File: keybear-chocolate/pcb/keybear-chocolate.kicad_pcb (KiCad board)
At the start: 2 copper layers, 151.4 x 117.1 mm, 95 parts, among them J1 MJ-4PP-9, J2 BATT, J3 LED, J4 OLED, SW1 SW_PUSH, SW10 SW_PUSH, SW11 SW_PUSH, SW12 SW_PUSH, SW13 SW_PUSH, SW14 SW_PUSH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

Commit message: adding more tracks
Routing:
- net VCC: track 2.64 -> 465.5 mm, vias 0 -> 25
- net Net-(L14-DIN): track 0.00 -> 39.0 mm, vias 0 -> 4
- net Net-(L14-DOUT): track 38.8 -> 53.7 mm, vias 2 -> 4
- net col2: track 215.5 -> 201.8 mm, vias 8 -> 7
- net Net-(L2-DIN): track 39.9 -> 46.3 mm, vias 2 -> 3
- net col0: track 238.3 -> 233.5 mm, vias 8 -> 7
- net col1: track 200.1 -> 195.7 mm, vias 8 -> 7
- net row2: track 182.1 -> 184.9 mm
- net row1: track 164.4 -> 162.2 mm
- net col4: track 148.2 -> 146.3 mm, vias 8 -> 7
- net ENCB: track 23.6 -> 21.9 mm
- net Net-(L1-DOUT): track 36.4 -> 35.1 mm
- net col3: track 154.6 -> 153.7 mm, vias 10 -> 9
- net Net-(L13-DIN): track 36.8 -> 35.9 mm
- net row0: track 177.3 -> 176.5 mm

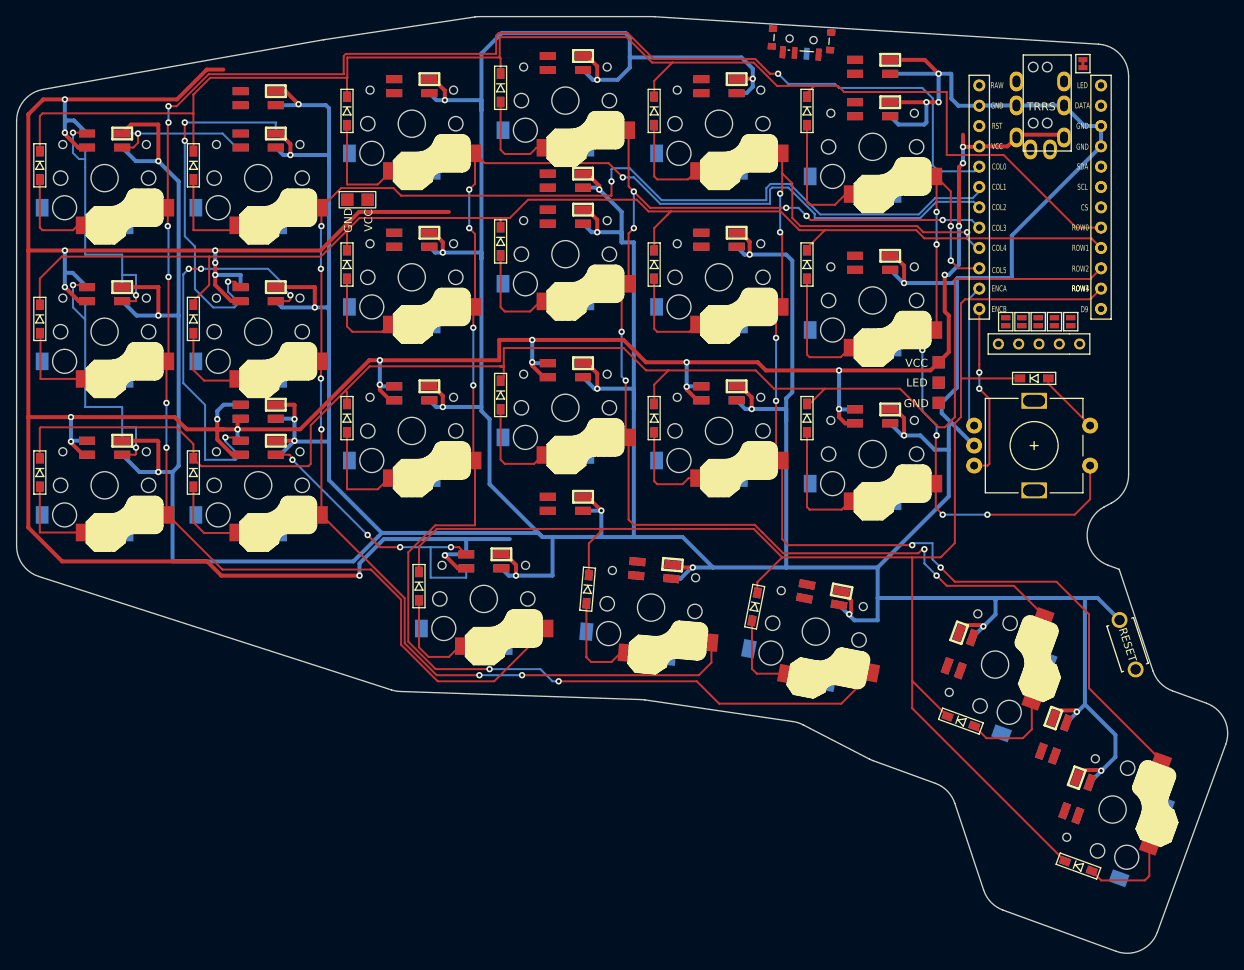
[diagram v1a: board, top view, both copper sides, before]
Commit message: more tracks added
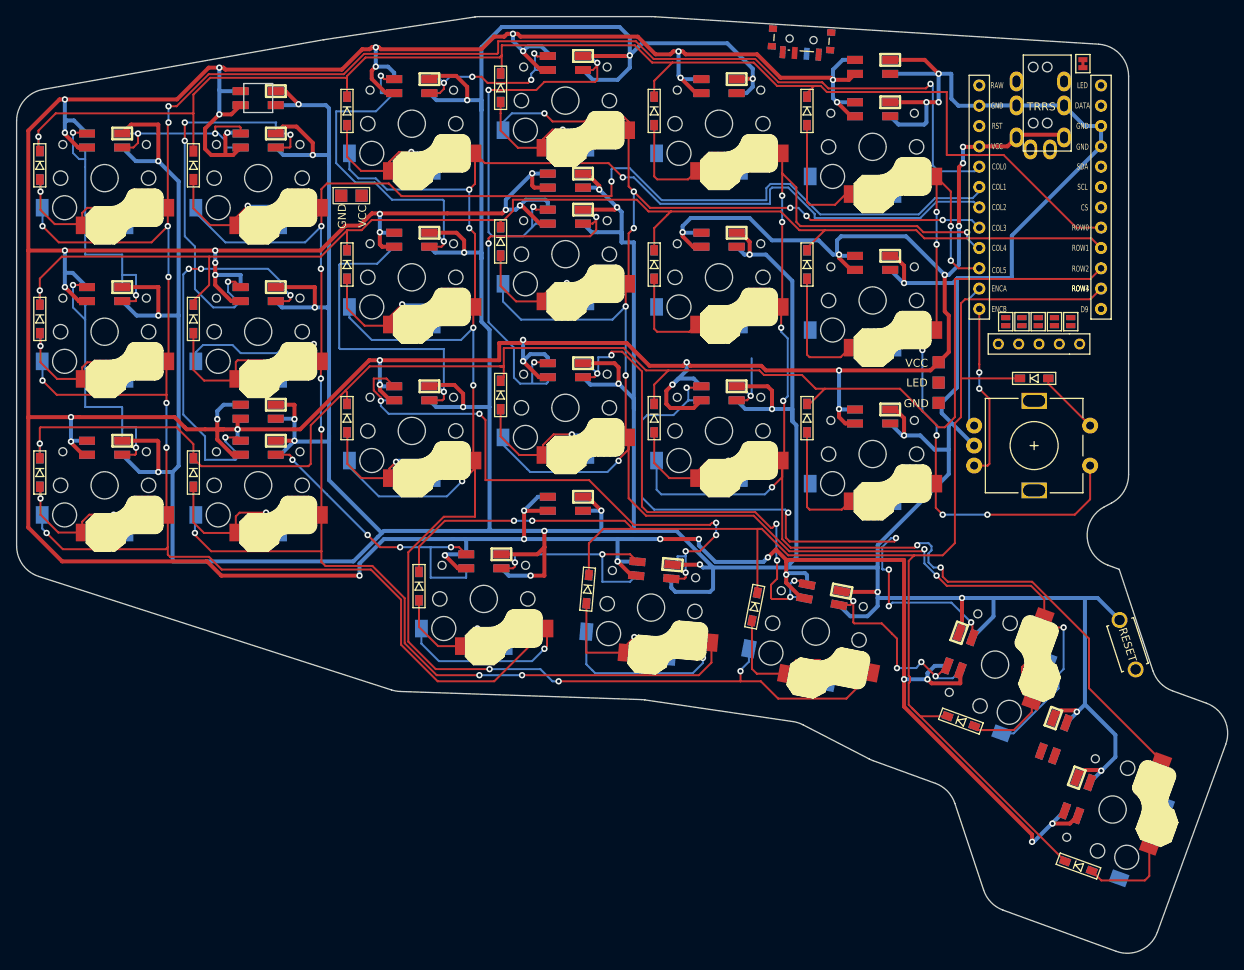
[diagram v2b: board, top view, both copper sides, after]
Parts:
- moved J2 0.92 mm to (179.6, 113.8)
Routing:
- net VCC: track 465.5 -> 861.8 mm, vias 25 -> 54
- net col1: track 195.7 -> 281.9 mm, vias 7 -> 10
- net Net-(L17-DOUT): track 0.00 -> 84.3 mm, vias 0 -> 6
- net col0: track 233.5 -> 313.5 mm, vias 7 -> 11
- net col3: track 153.7 -> 232.6 mm, vias 9 -> 12
- net Net-(L15-DOUT): track 0.00 -> 75.0 mm, vias 0 -> 6
- net Net-(L16-DIN): track 0.00 -> 67.0 mm, vias 0 -> 6
- net col2: track 201.8 -> 262.4 mm, vias 7 -> 9
- net Net-(L10-DOUT): track 0.00 -> 51.6 mm, vias 0 -> 3
- net Net-(L10-DIN): track 0.00 -> 48.3 mm, vias 0 -> 3
- net Net-(L3-DOUT): track 0.00 -> 45.8 mm, vias 0 -> 2
- net Net-(L15-DIN): track 0.00 -> 41.5 mm, vias 0 -> 1
- net GND: track 877.5 -> 910.2 mm, vias 30 -> 31
- net Net-(L19-DIN): track 0.00 -> 28.8 mm, vias 0 -> 2
- net Net-(L21-DIN): track 0.00 -> 28.4 mm, vias 0 -> 4
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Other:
- outline, holes or cut-outs redrawn

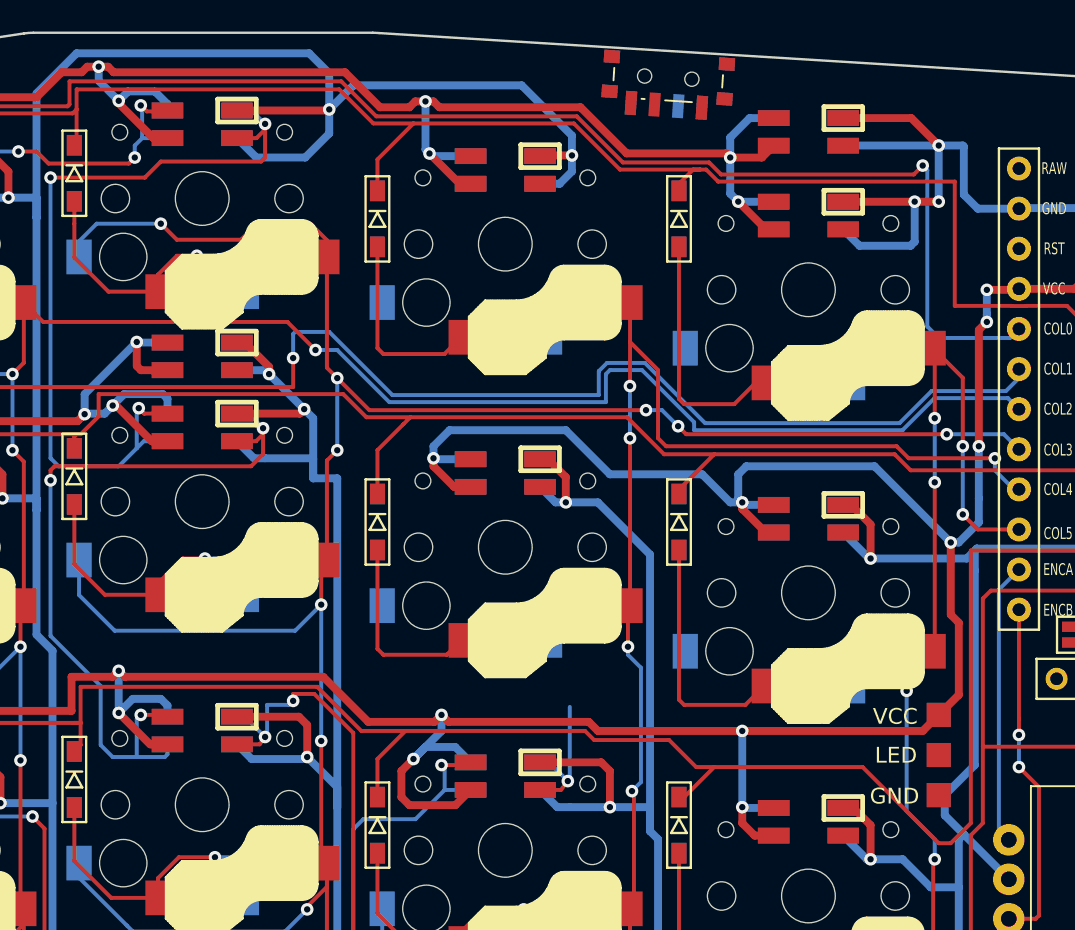
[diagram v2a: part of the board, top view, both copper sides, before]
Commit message: more tracks added
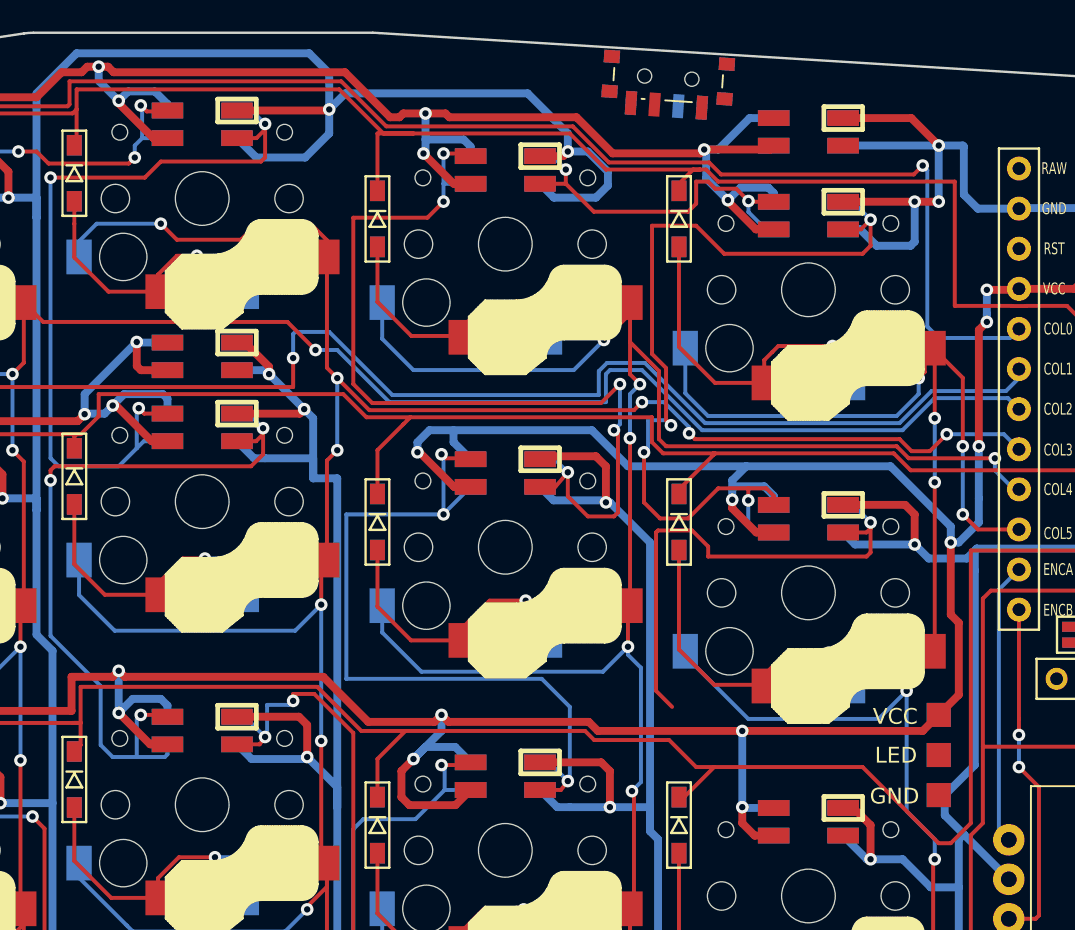
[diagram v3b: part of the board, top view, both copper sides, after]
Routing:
- net Net-(L11-DIN): track 0.00 -> 59.5 mm, vias 0 -> 5
- net Net-(L12-DOUT): track 0.00 -> 55.7 mm, vias 0 -> 4
- net col4: track 168.5 -> 208.9 mm, vias 8 -> 9
- net Net-(L11-DOUT): track 9.16 -> 49.0 mm, vias 1 -> 3
- net SW24A: track 82.9 -> 121.7 mm, vias 8 -> 9
- net Net-(L12-DIN): track 0.00 -> 32.7 mm, vias 0 -> 1
- net Net-(L5-DIN): track 0.00 -> 23.3 mm, vias 0 -> 2
- net GND: track 910.2 -> 920.5 mm
- net VCC: track 861.8 -> 869.6 mm
- net Net-(D6-A): track 15.7 -> 22.4 mm, vias 0 -> 1
- net Net-(D11-A): track 12.1 -> 18.6 mm, vias 0 -> 1
- net Net-(D5-A): track 12.3 -> 18.5 mm, vias 0 -> 1
- net Net-(D12-A): track 15.5 -> 21.6 mm, vias 0 -> 1
- net col3: track 232.6 -> 234.2 mm
- net row1: track 164.6 -> 165.5 mm
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
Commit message: finished with keys LEG's tracks
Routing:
- net Net-(L25-DIN): track 0.00 -> 103.7 mm, vias 0 -> 4
- net Net-(L18-DIN): track 0.00 -> 94.4 mm, vias 0 -> 5
- net VCC: track 869.6 -> 892.9 mm, vias 54 -> 55
- net Net-(L12-DIN): track 32.7 -> 54.8 mm, vias 1 -> 3
- net col4: track 208.9 -> 230.2 mm, vias 9 -> 10
- net SW24A: track 121.7 -> 141.3 mm, vias 9 -> 10
- net Net-(L23-DIN): track 0.00 -> 13.7 mm, vias 0 -> 2
- net GND: track 920.5 -> 928.8 mm, vias 31 -> 32
- net Net-(D23-A): track 11.6 -> 19.3 mm, vias 0 -> 1
- net Net-(D18-A): track 15.3 -> 21.4 mm, vias 0 -> 1
- net Net-(L11-DOUT): track 49.0 -> 45.6 mm
- net row2: track 186.7 -> 183.5 mm

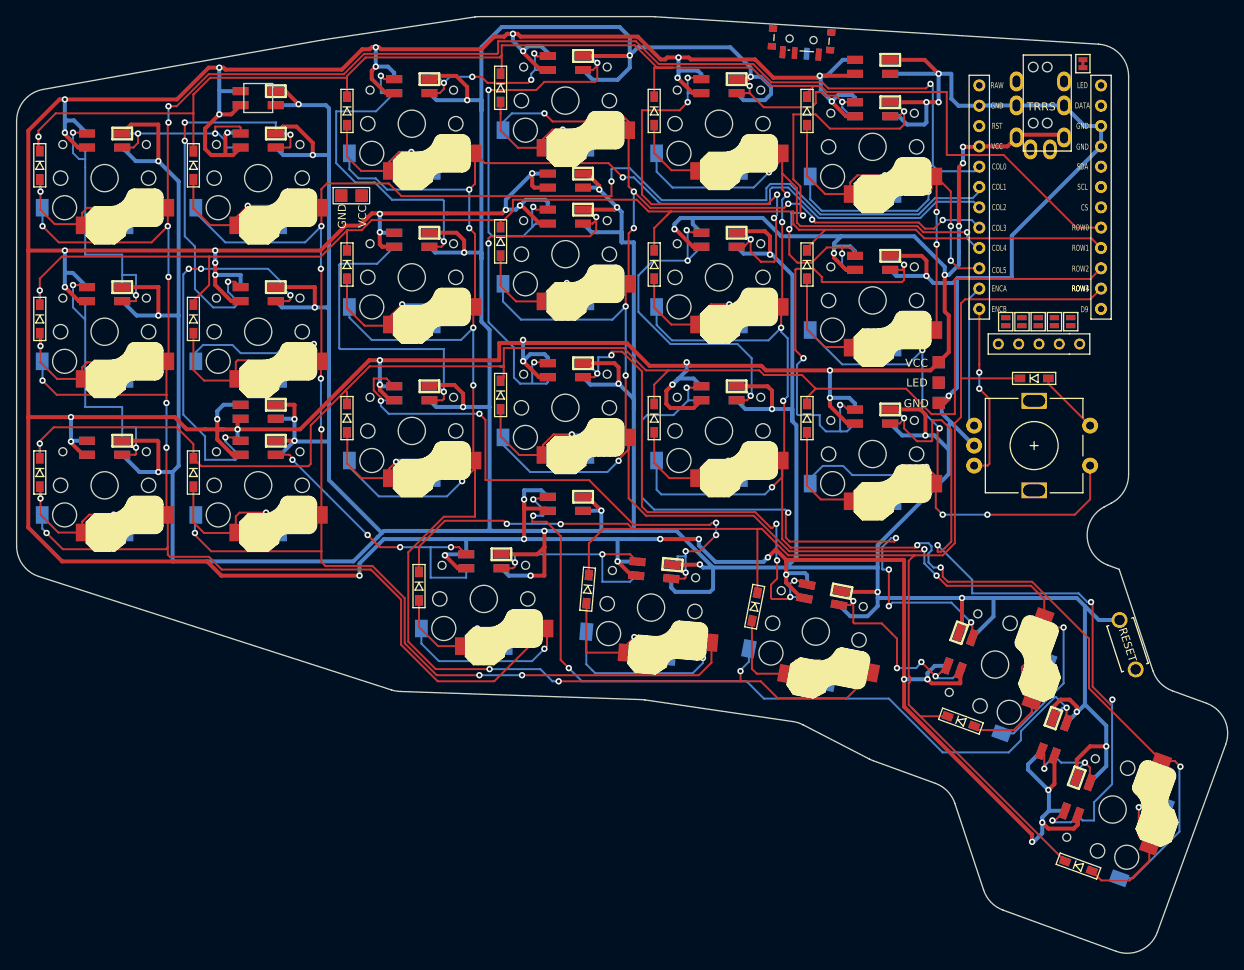
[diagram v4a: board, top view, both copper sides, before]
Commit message: finishing back leds
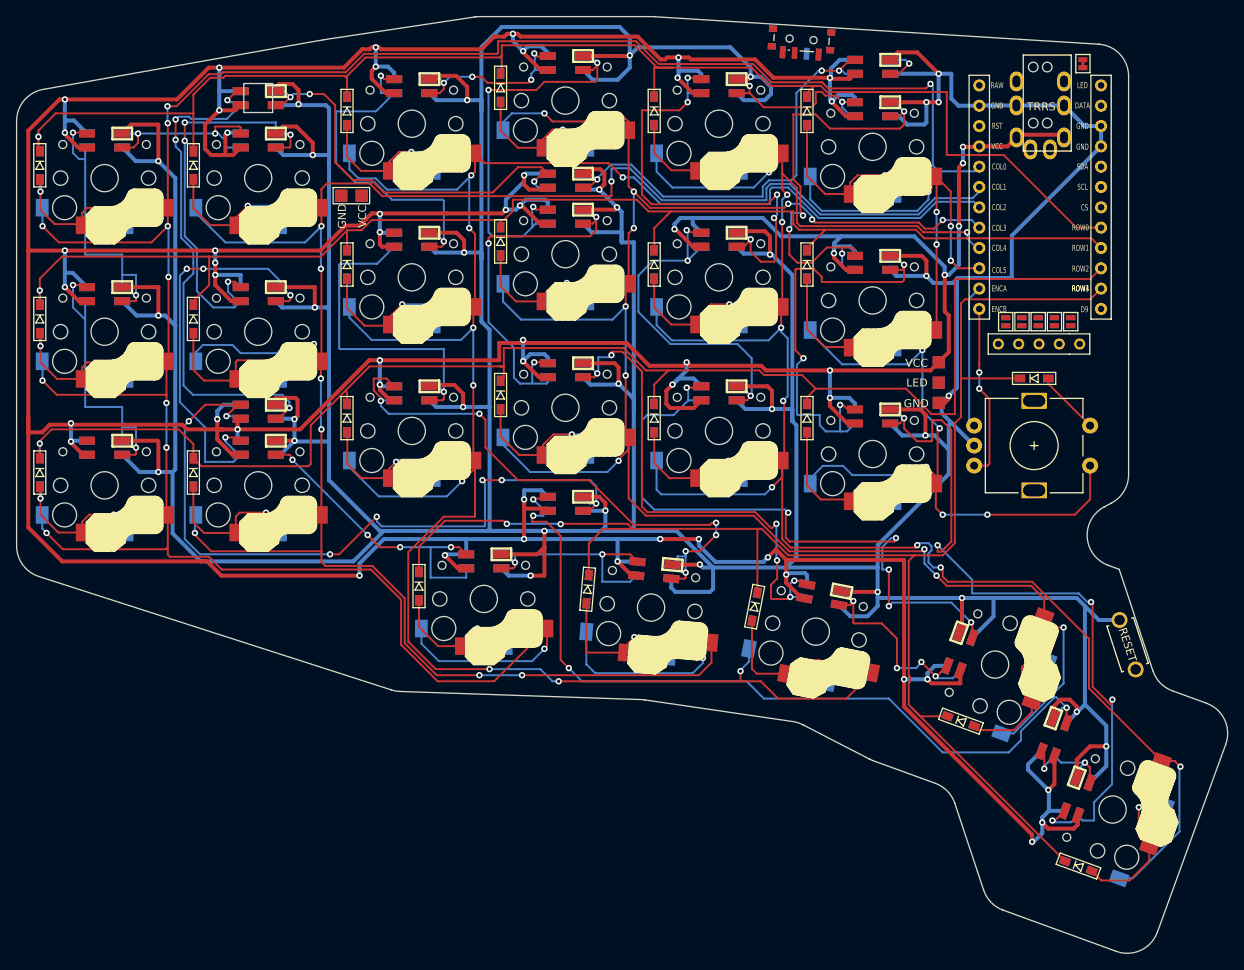
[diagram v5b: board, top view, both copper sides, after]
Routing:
- net Net-(L26-DIN): track 0.00 -> 94.6 mm, vias 0 -> 7
- net Net-(L27-DIN): track 0.00 -> 66.9 mm, vias 0 -> 4
- net Net-(L29-DIN): track 0.00 -> 55.3 mm, vias 0 -> 3
- net Net-(L28-DIN): track 0.00 -> 51.9 mm, vias 0 -> 3
- net GND: track 928.8 -> 935.7 mm
- net LED: track 0.00 -> 5.47 mm, vias 0 -> 1
- net Net-(L15-DOUT): track 75.0 -> 72.6 mm
- net col2: track 262.1 -> 263.0 mm
- net VCC: track 892.9 -> 893.9 mm
- net Net-(L14-DOUT): track 53.7 -> 54.5 mm

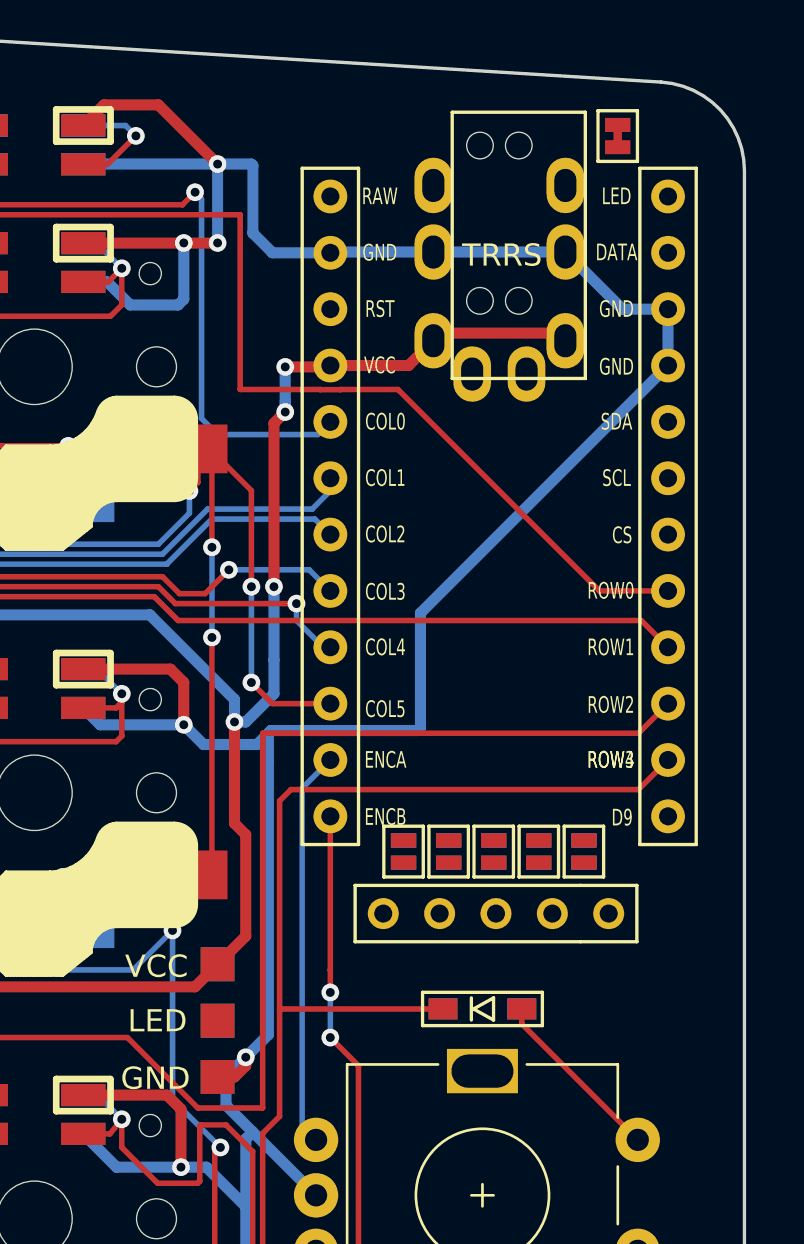
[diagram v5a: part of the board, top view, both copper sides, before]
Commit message: LEDs connected
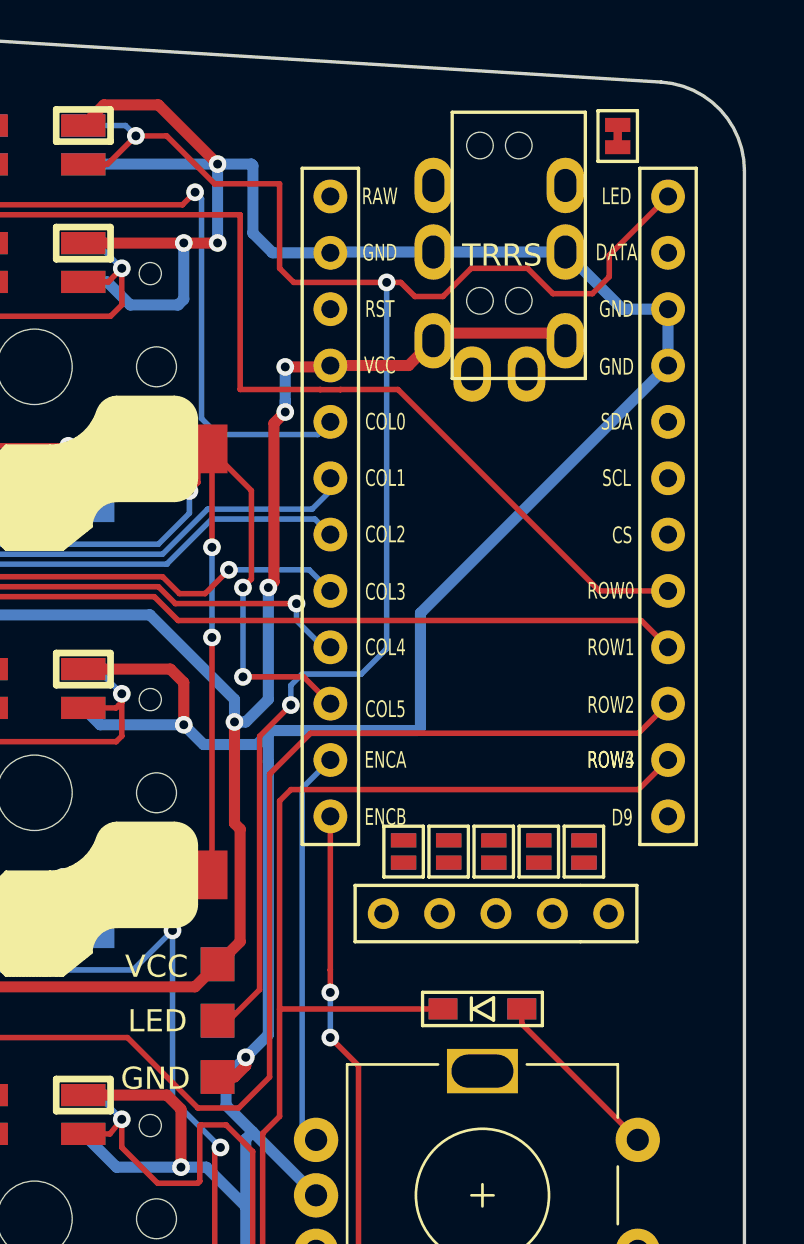
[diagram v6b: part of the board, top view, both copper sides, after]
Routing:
- net LED: track 5.47 -> 76.3 mm, vias 1 -> 3
- net row2: track 183.3 -> 181.4 mm
